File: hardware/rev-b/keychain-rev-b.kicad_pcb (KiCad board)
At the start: 4 copper layers, 30 x 52.5 mm, 58 parts, among them J1 USB-C, J2 OLED 0.96" I2C, J3 SWD, M1 вибромотор 0820, Q1 AO3401A, Q2 AO3401A, Q3 AO3400A, Q4 AO3400A, SW1 B3U-3100P, U1 MDBT50Q-1MV2, U2 MCP73832-2, U3 USBLC6-2SC6, U4 LIS3DH, U5 LTR-303ALS-01, U6 SPH0641LM4H-1

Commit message: Черновик: исправления по полному предрелизному аудиту (в работе)
Промежуточное состояние, пока идут трассировка платы и параллельные правки:
- плата: SA0 акселерометра на VDD, C6 4.7 мкФ, C14/C15 100 нФ, перемычки экрана
  дальше от штырей, R3 на ножку CHG_EN (заряд по температуре), R20 47 кОм, TVS D3 и
  10 Ом к VBUS модуля, 100 Ом в линиях SWD, шире запретная зона антенны, без пасты
  на площадках проводов; расстановка обновлена, трассировка ещё не сделана;
- прошивка: адрес LIS3DH 0x19 и отключение подтяжки, разрешение заряда, восстановление
  датчиков и экрана, батарея после отключения USB, загрузчик по кнопке + USB, сутки
  без часов, журнал с длинами частей и др.;
- движок: батарея, дружба после дуэли, недостижимые эмоции, походка.

Файлы для завода в out/ ещё старые — будут пересобраны после трассировки.

Co-Authored-By: Claude Opus 5.5 <noreply@anthropic.com>
Claude-Session: https://claude.ai/code/session_01RQ7GfaTDyVK1Dcdo3sKM8F
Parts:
- added D3: SMF5.0A, Diode_SMD:D_SOD-123F, B.Cu at (7.30, 43.2)
- added R21: 10R, Resistor_SMD:R_0402_1005Metric, F.Cu at (11.8, 11.4)
- added R22: 100R, Resistor_SMD:R_0402_1005Metric, F.Cu at (21.6, 13.6)
- added R23: 100R, Resistor_SMD:R_0402_1005Metric, F.Cu at (23.2, 13.6)
- C14, C15: value 1uF -> 100nF
- C6: value 10uF -> 4.7uF
- R20: value 100k -> 47k
- moved R16 1.40 mm to (10.4, 23.0)
- moved R17 1.40 mm to (12.0, 23.0)
- moved R18 1.40 mm to (13.4, 23.0)
- moved R19 1.40 mm to (15.0, 23.0)
- moved R8 0.15 mm to (5.70, 13.1)
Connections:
- C8 pad 1: VBUS -> VBUS_NRF
- J3 pad 2: SWDIO -> SWDIO_J
- J3 pad 4: SWDCLK -> SWDCLK_J
- R3 pad 2: GND -> CHG_EN
- U1 pad 32: VBUS -> VBUS_NRF
- U1 pad 45: (no net) -> CHG_EN
- U4 pad 7: GND -> VDD
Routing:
- net VDD: track 131.0 -> 0.00 mm, vias 14 -> 0
- net VSYS: track 124.7 -> 0.00 mm, vias 11 -> 0
- net VBUS: track 82.1 -> 0.00 mm, vias 11 -> 0
- net VBAT: track 47.4 -> 0.00 mm, vias 4 -> 0
- net USB_DN: track 46.1 -> 0.00 mm, vias 1 -> 0
- net GND: track 44.4 -> 0.00 mm, vias 44 -> 0
- net CHG_IO: track 36.6 -> 0.00 mm, vias 1 -> 0
- net DISP_EN: track 35.3 -> 0.00 mm, vias 1 -> 0
- net USB_DP: track 34.0 -> 0.00 mm, vias 1 -> 0
- net ACC_INT1: track 24.8 -> 0.00 mm, vias 1 -> 0
- net MIC_PWR: track 23.7 -> 0.00 mm, vias 4 -> 0
- net SENS_SCL: track 23.4 -> 0.00 mm, vias 1 -> 0
- net VIB_EN: track 22.9 -> 0.00 mm, vias 1 -> 0
- net BTN: track 21.0 -> 0.00 mm, vias 1 -> 0
- net SENS_SDA: track 19.6 -> 0.00 mm, vias 1 -> 0
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- removed copper zone on B.Cu, net GND
- removed copper zone on F.Cu, net GND
- removed copper zone on In1.Cu, net GND
- removed copper zone on In2.Cu, net GND

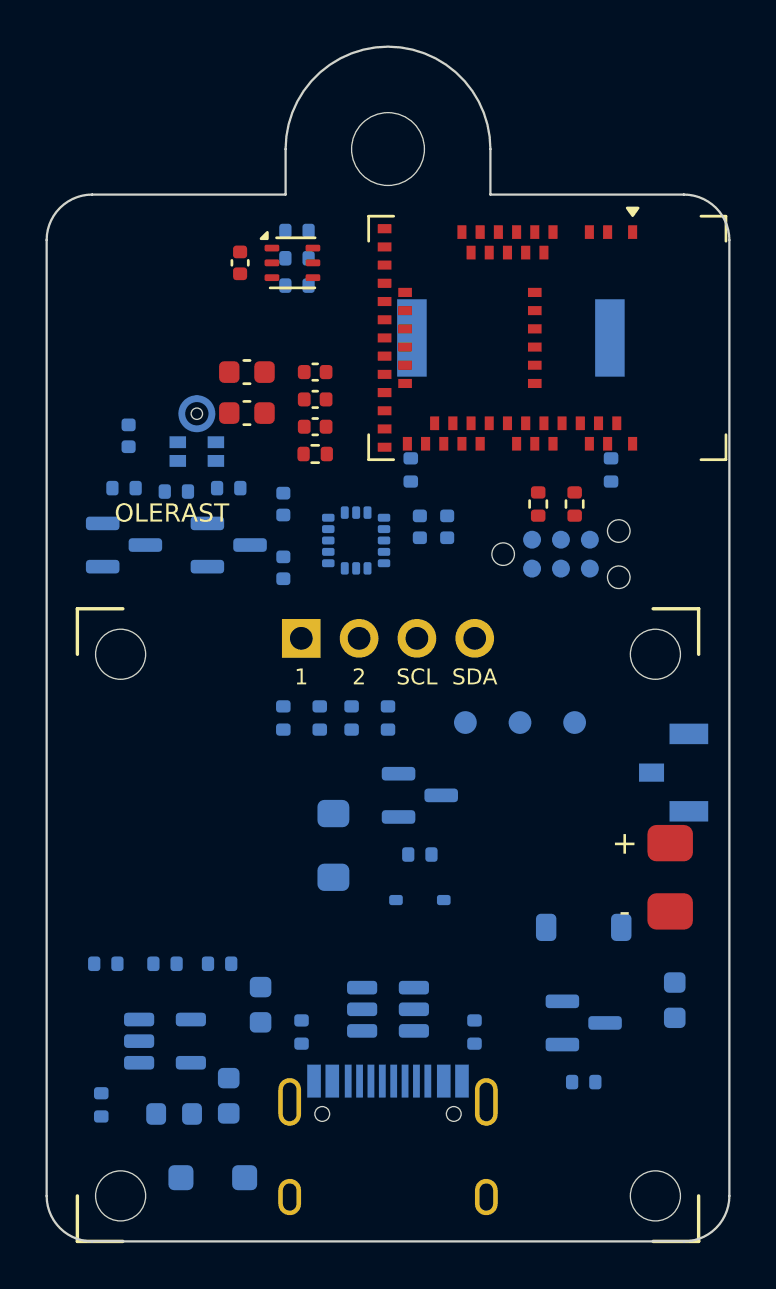
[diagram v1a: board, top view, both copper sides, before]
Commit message: Черновик: плата — R21, R22/R23 на обороте, доводка без переходных в площадках (в работе)
- R21 (10 Ом к VBUS модуля) и R22/R23 (100 Ом в SWD) перенесены на оборот: на лицевой
  стороне они перекрывали проходы у нижнего ряда выводов модуля, и четыре цепи не
  разводились;
- D3 повёрнут, чтобы не задевать зону стойки экрана; R8 — на прежнем месте;
- доводка трассировки (fixroute.py) больше не ставит переходное отверстием в SMD-площадку
  своей цепи;
- промежуточные правки исполнителей (движок, прошивка, корпус, документы).

Трассировка ещё идёт, файлы для завода — старые.

Co-Authored-By: Claude Opus 5.5 <noreply@anthropic.com>
Claude-Session: https://claude.ai/code/session_01RQ7GfaTDyVK1Dcdo3sKM8F
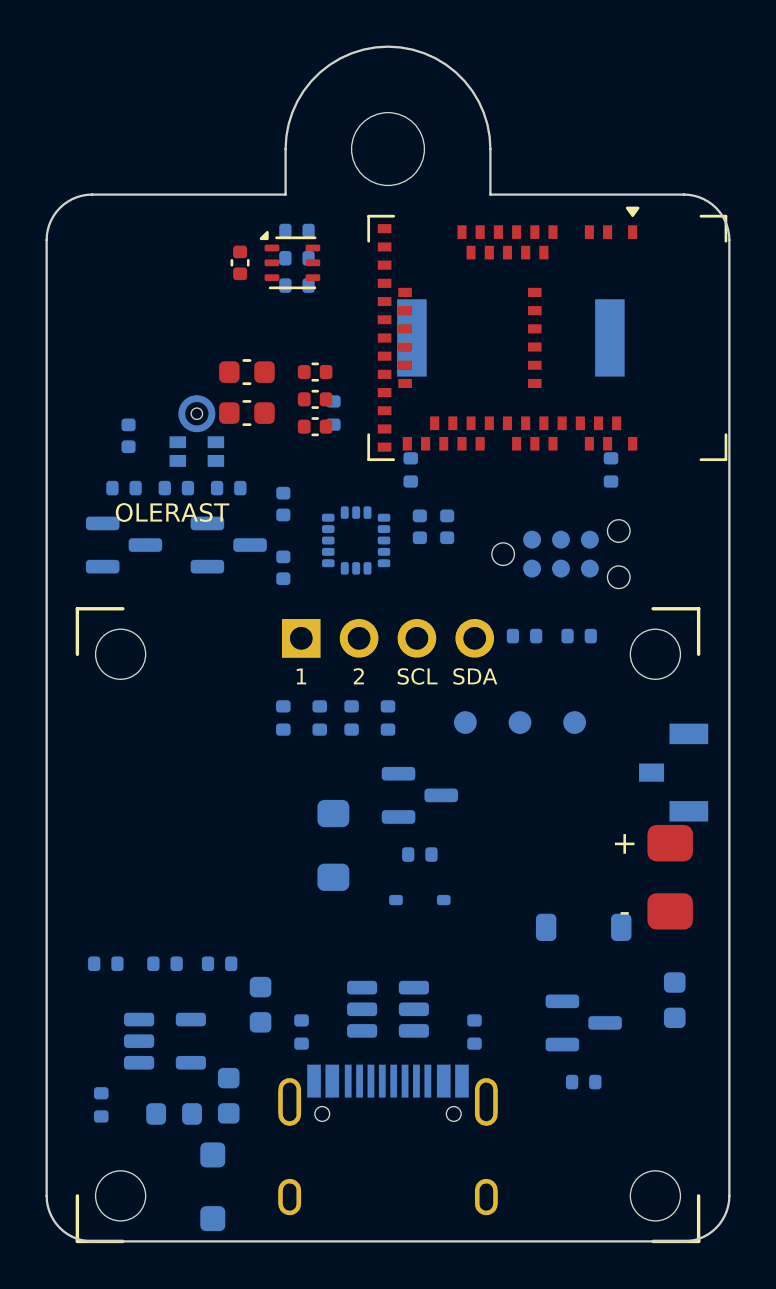
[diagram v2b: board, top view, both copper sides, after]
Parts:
- R21, R22, R23: moved to B.Cu
- moved R22 5.83 mm to (21.0, 19.4), turned to 0 degrees
- moved R23 5.80 mm to (23.4, 19.4), turned to 0 degrees
- moved R21 1.97 mm to (12.6, 9.60), turned to 90 degrees
- moved D3 0.40 mm to (7.30, 43.6), turned to 90 degrees
- moved R8 0.15 mm to (5.70, 12.9)
